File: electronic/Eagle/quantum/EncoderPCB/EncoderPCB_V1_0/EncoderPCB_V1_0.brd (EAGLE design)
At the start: 38.1 x 68.2 mm, 15 parts, among them IC1 STM32F031K6T7

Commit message: Encoder PCB_V1_0 fertiggestellt
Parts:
- removed C5: 100nF, C_Sager_Bibliothek:C0603
- removed C6: 1µF, C_Sager_Bibliothek:153CLV-0605
- removed C7: 4,7µF, C_Sager_Bibliothek:153CLV-0605
- removed U$1, U$2, U$3: TPTHT, C_Sager_Bibliothek:THT_PIN
- added 3V1, GND, GND2, I2C1_SCL, I2C1_SDA, NRST, SWCLK, SWDIO, USART1_RX1, USART1_TX: TPTHT, C_Sager_Bibliothek:THT_PIN
- added R1, R11: 10k, C_Sager_Bibliothek:R0805
- added R10, R2, R3, R4, R5, R6, R7, R8, R9: (no value), C_Sager_Bibliothek:R0805
- IC1: value STM32F031K6T7 -> STM32F031K6T6; device C_Sager_Bibliothek:QFP50P900X900X160-48N -> C_Sager_Bibliothek:QFP80P900X900X160-32N
- moved C8 42.4 mm to (22.3, 53.7), flipped to the bottom, turned to 270 degrees
- moved C4 21.1 mm to (24.6, 47.3), flipped to the bottom
- moved C1 18.6 mm to (14.9, 39.0), flipped to the bottom, turned to 270 degrees
- moved C2 18.3 mm to (14.9, 35.5), flipped to the bottom, turned to 90 degrees
- moved IC1 16.4 mm to (22.1, 39.2), flipped to the bottom, turned to 180 degrees
- moved C3 16.0 mm to (27.0, 47.9), flipped to the bottom, turned to 90 degrees
- moved S3 4.51 mm to (10.0, 12.0)
- moved S2 4.29 mm to (10.0, 30.0)
- moved S1 4.07 mm to (10.0, 48.0)
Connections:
- new net ADRR.: IC1.3, R1.2
- new net BOOT_0: IC1.31, R11.2
- new net BUTTON_ENC1: IC1.28, S1.3
- new net BUTTON_ENC2: IC1.30, S2.3
- new net BUTTON_ENC3: IC1.2, S3.3
- new net B_ENC1: IC1.11, R4.1
- new net B_ENC2: IC1.14, R7.1
- new net B_ENC3: IC1.27, R10.1
- new net ENCODER1_A: IC1.18, S1.A1
- new net ENCODER1_B: IC1.19, S1.B1
- new net ENCODER2_A: IC1.6, S2.A1
- new net ENCODER2_B: IC1.7, S2.B1
- new net ENCODER3_A: IC1.12, S3.A1
- new net ENCODER3_B: IC1.13, S3.B1
- new net G_ENC1: IC1.10, R3.1
- new net G_ENC2: IC1.22, R6.1
- new net G_ENC3: IC1.26, R9.1
- new net I2C1_SCL: I2C1_SCL.P$1, IC1.29
- new net I2C1_SDA: I2C1_SDA.P$1, IC1.20
- new net N$10: R3.2, S1.2
- new net N$11: R5.2, S2.1
- new net N$12: R4.2, S1.4
- new net N$13: R6.2, S2.2
- new net N$14: R7.2, S2.4
- new net N$15: R8.2, S3.1
- new net N$16: R9.2, S3.2
- new net N$17: R10.2, S3.4
- new net N$9: R2.2, S1.1
- new net NRST: IC1.4, NRST.P$1
- new net R_ENC1: IC1.9, R2.1
- new net R_ENC2: IC1.21, R5.1
- new net R_ENC3: IC1.15, R8.1
- new net SWCLK: IC1.24, SWCLK.P$1
- new net SWDIO: IC1.23, SWDIO.P$1
- new net USART1_RX1: IC1.25, USART1_RX1.P$1
- new net USART1_TX: IC1.8, USART1_TX.P$1
- net +3V3: now also 3V1.P$1, IC1.17, IC1.5, S1.5, S2.5, S3.5; no longer C5.1, C6.+, C7.+, IC1.24, IC1.48, IC1.9
- net GND: now also GND.P$1, GND2.P$1, IC1.16, IC1.32, R1.1, R11.1, S1.C1, S2.C1, S3.C1; no longer C5.2, C6.-, C7.-, IC1.23, IC1.47, IC1.8
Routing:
- net GND: track 0.00 -> 65.7 mm, vias 0 -> 6
- net B_ENC3: track 0.00 -> 51.1 mm, vias 0 -> 2
- net BUTTON_ENC3: track 0.00 -> 43.3 mm, vias 0 -> 3
- net BUTTON_ENC2: track 0.00 -> 42.9 mm, vias 0 -> 1
- net R_ENC3: track 0.00 -> 42.3 mm, vias 0 -> 4
- net G_ENC3: track 0.00 -> 40.3 mm, vias 0 -> 2
- net ENCODER3_A: track 0.00 -> 39.6 mm, vias 0 -> 3
- net SWDIO: track 0.00 -> 36.9 mm, vias 0 -> 2
- net B_ENC2: track 0.00 -> 36.6 mm, vias 0 -> 2
- net ENCODER3_B: track 0.00 -> 35.2 mm, vias 0 -> 2
- net NRST: track 0.00 -> 34.9 mm, vias 0 -> 1
- net SWCLK: track 0.00 -> 33.7 mm, vias 0 -> 2
- net USART1_TX: track 0.00 -> 31.6 mm, vias 0 -> 1
- net BUTTON_ENC1: track 0.00 -> 29.7 mm, vias 0 -> 1
- net G_ENC2: track 0.00 -> 29.2 mm, vias 0 -> 2
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- added copper zone on layer 16, net +3V3
- added copper zone on layer 1, net GND
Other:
- board size 38.1 x 68.2 mm -> 30 x 60 mm
- board text added: "+3V3"
- board text added: "GND"
- board text added: "NRST"
- board text added: "RX"
- board text added: "SCL"
- board text added: "SDA"
- board text added: "SWCLK"
- board text added: "SWDIO"
- board text added: "TX"

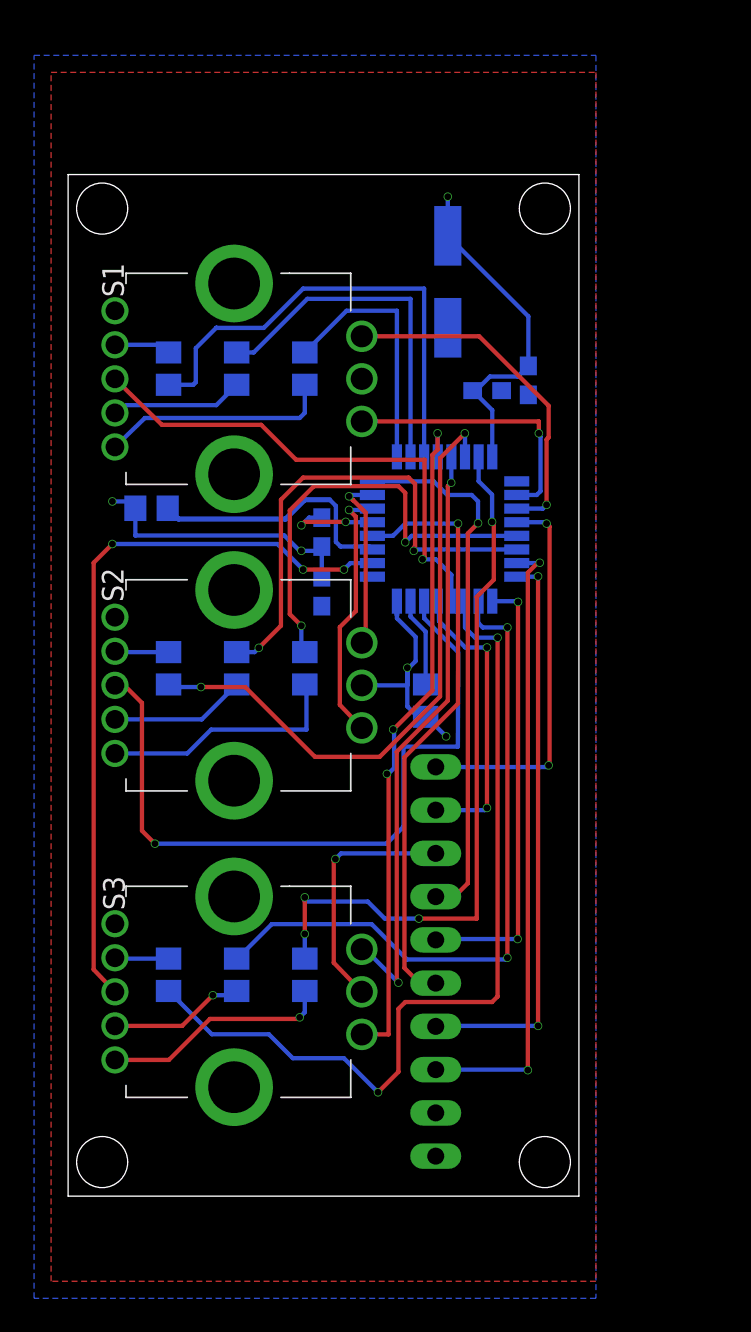
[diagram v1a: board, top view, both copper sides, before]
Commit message: Finalized Encoder_V1_0; New Front/Backpanel; Started quantum_PSU
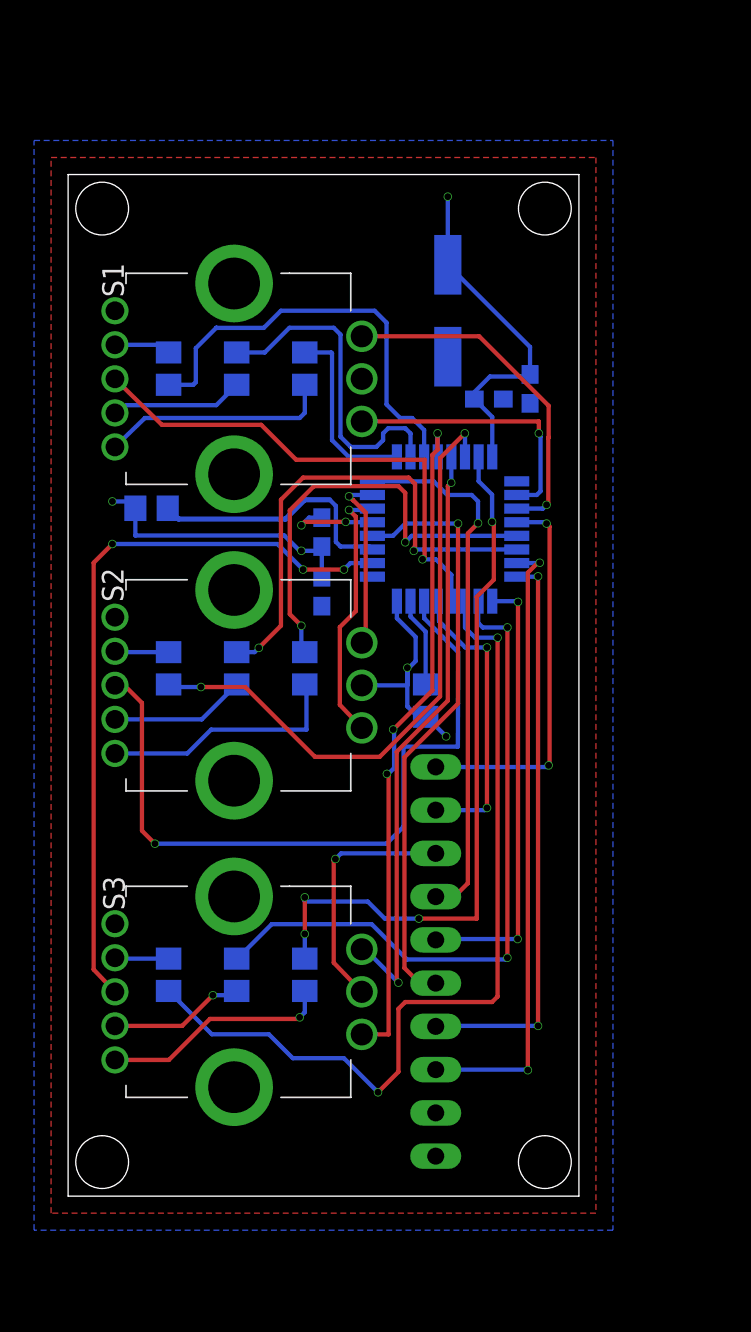
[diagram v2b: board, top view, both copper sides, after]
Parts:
- moved C8 1.70 mm to (22.3, 52.0)
- moved C4 0.51 mm to (24.7, 46.8)
- moved C3 0.51 mm to (27.1, 47.4)
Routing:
- net R_ENC1: track 15.0 -> 10.9 mm
- net B_ENC1: track 28.4 -> 25.3 mm
- net G_ENC1: track 20.8 -> 19.4 mm
- net GND: track 65.7 -> 65.1 mm
